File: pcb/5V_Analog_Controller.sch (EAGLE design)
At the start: 22 parts, among them J1 POWER, Q1 AO3400, Q2 AO3400, U1 ESP32-PICO-MINI-02, U2 AP2112K, X1 PROG, X2 SS-52100-001, X3 SS-52100-001, X5 BOOT, X6 RESET

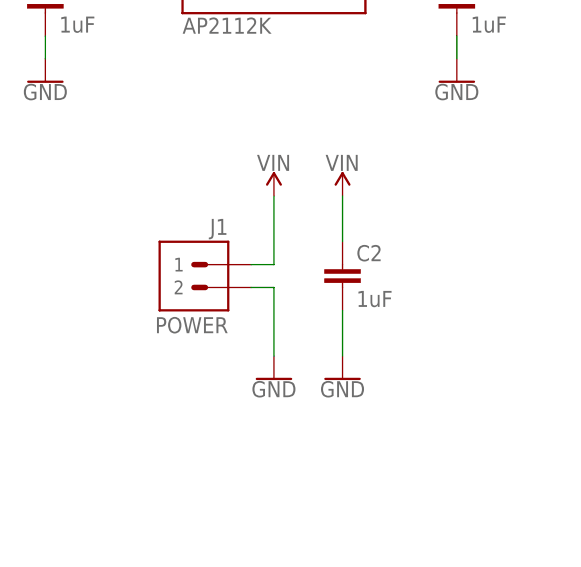
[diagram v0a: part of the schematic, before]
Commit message: Switch to input power jack
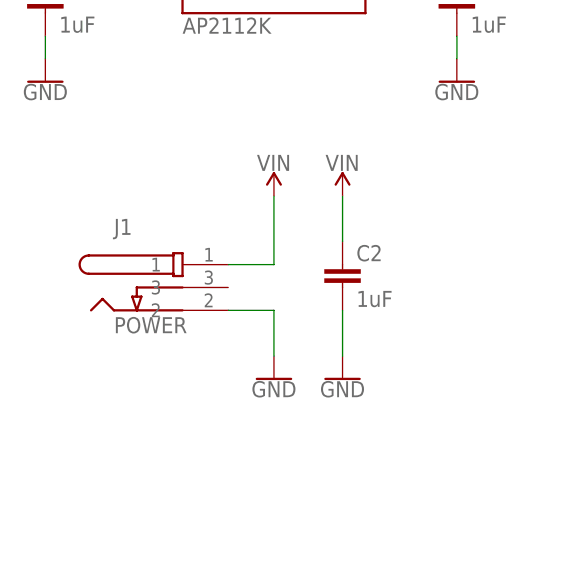
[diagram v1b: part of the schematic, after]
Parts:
- J1: device M2M-Connectors:TERMINAL-1X02-2.54P -> M2M-Connectors:XKB-DC-005-5A-2.0
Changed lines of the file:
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@@
 <part name="GND10" library="M2M-Power" deviceset="GND" device=""/>
 <part name="SUPPLY6" library="M2M-Power" deviceset="VCC" device=""/>
-<part name="J1" library="M2M-Connectors" deviceset="TERMINAL-1X02-2.54" device="P" value="POWER"/>
+<part name="J1" library="M2M-Connectors" deviceset="XKB-DC-005-5A-2.0" device="" value="POWER"/>
 <part name="U2" library="M2M-IC" deviceset="REGULATOR-AP2112K" device="K-SOT23-5" value="AP2112K"/>
 <part name="SUPPLY2" library="M2M-Power" deviceset="VIN" device=""/>
@@
 <attribute name="VALUE" x="160.02" y="160.274" size="1.778" layer="96" align="bottom-center"/>
 </instance>
-<instance part="J1" gate="G$1" x="43.18" y="111.76" smashed="yes" rot="MR0">
-<attribute name="VALUE" x="45.72" y="106.68" size="1.778" layer="96" rot="MR0"/>
-<attribute name="NAME" x="45.72" y="117.602" size="1.778" layer="95" rot="MR0"/>
+<instance part="J1" gate="G$1" x="35.56" y="111.76" smashed="yes">
+<attribute name="VALUE" x="33.02" y="106.68" size="1.778" layer="96"/>
+<attribute name="NAME" x="33.02" y="117.602" size="1.778" layer="95"/>
 </instance>
 <instance part="U2" gate="G$1" x="50.8" y="147.32" smashed="yes">
@@
 <segment>
 <pinref part="GND6" gate="1" pin="GND"/>
-<wire x1="48.26" y1="111.76" x2="50.8" y2="111.76" width="0.1524" layer="91"/>
-<wire x1="50.8" y1="111.76" x2="50.8" y2="104.14" width="0.1524" layer="91"/>
+<wire x1="45.72" y1="109.22" x2="50.8" y2="109.22" width="0.1524" layer="91"/>
+<wire x1="50.8" y1="109.22" x2="50.8" y2="104.14" width="0.1524" layer="91"/>
 <pinref part="J1" gate="G$1" pin="2"/>
 </segment>
@@
 <net name="VIN" class="0">
 <segment>
-<wire x1="48.26" y1="114.3" x2="50.8" y2="114.3" width="0.1524" layer="91"/>
+<wire x1="45.72" y1="114.3" x2="50.8" y2="114.3" width="0.1524" layer="91"/>
 <wire x1="50.8" y1="114.3" x2="50.8" y2="121.92" width="0.1524" layer="91"/>
 <pinref part="J1" gate="G$1" pin="1"/>

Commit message: Add reverse power protection for internal circuits
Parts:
- added D1: B5819LW, M2M-DiscreteSemi:DIODE-SCHOTTKYSOD-123
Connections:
- new net VSW: D1.A, F1.1, F2.1, J1.1
- net VIN: now also D1.C; no longer F1.1, F2.1, J1.1
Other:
- moved on the sheet: J1
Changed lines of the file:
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@@
 <part name="GND11" library="M2M-Power" deviceset="GND" device=""/>
 <part name="SUPPLY8" library="M2M-Power" deviceset="VCC" device=""/>
-<part name="SUPPLY3" library="M2M-Power" deviceset="VIN" device=""/>
-<part name="SUPPLY4" library="M2M-Power" deviceset="VIN" device=""/>
 <part name="SUPPLY5" library="M2M-Power" deviceset="VIN" device=""/>
 <part name="R3" library="M2M-Passives" deviceset="RESISTOR" device="0603" value="10K"/>
@@
 <part name="F1" library="M2M-Fuse" deviceset="PTC" device="JK-SMD300" value="JK-SMD300L-16"/>
 <part name="F2" library="M2M-Fuse" deviceset="PTC" device="JK-SMD300" value="JK-SMD300L-16"/>
+<part name="D1" library="M2M-DiscreteSemi" deviceset="DIODE-SCHOTTKY" device="SOD-123" value="B5819LW"/>
+<part name="SUPPLY3" library="M2M-Power" deviceset="VSW" device=""/>
+<part name="SUPPLY4" library="M2M-Power" deviceset="VSW" device=""/>
+<part name="SUPPLY11" library="M2M-Power" deviceset="VSW" device=""/>
 </parts>
 <sheets>
@@
 <attribute name="VALUE" x="160.02" y="160.274" size="1.778" layer="96" align="bottom-center"/>
 </instance>
-<instance part="J1" gate="G$1" x="35.56" y="111.76" smashed="yes">
-<attribute name="VALUE" x="33.02" y="106.68" size="1.778" layer="96"/>
-<attribute name="NAME" x="33.02" y="117.602" size="1.778" layer="95"/>
+<instance part="J1" gate="G$1" x="20.32" y="111.76" smashed="yes">
+<attribute name="VALUE" x="17.78" y="106.68" size="1.778" layer="96"/>
+<attribute name="NAME" x="17.78" y="117.602" size="1.778" layer="95"/>
 </instance>
 <instance part="U2" gate="G$1" x="50.8" y="147.32" smashed="yes">
@@
 <attribute name="VALUE" x="71.12" y="157.734" size="1.778" layer="96" align="bottom-center"/>
 </instance>
-<instance part="SUPPLY3" gate="G$1" x="182.88" y="147.32" smashed="yes">
-<attribute name="VALUE" x="182.88" y="150.114" size="1.778" layer="96" align="bottom-center"/>
-</instance>
-<instance part="SUPPLY4" gate="G$1" x="182.88" y="91.44" smashed="yes">
-<attribute name="VALUE" x="182.88" y="94.234" size="1.778" layer="96" align="bottom-center"/>
-</instance>
 <instance part="SUPPLY5" gate="G$1" x="58.42" y="121.92" smashed="yes">
 <attribute name="VALUE" x="58.42" y="124.714" size="1.778" layer="96" align="bottom-center"/>
@@
 <attribute name="NAME" x="187.96" y="88.646" size="1.778" layer="95"/>
 <attribute name="VALUE" x="187.96" y="82.296" size="1.778" layer="95"/>
+</instance>
+<instance part="D1" gate="G$1" x="40.64" y="114.3" smashed="yes">
+<attribute name="NAME" x="36.83" y="116.078" size="1.778" layer="95"/>
+<attribute name="VALUE" x="36.83" y="110.744" size="1.778" layer="96"/>
+</instance>
+<instance part="SUPPLY3" gate="G$1" x="33.02" y="121.92" smashed="yes">
+<attribute name="VALUE" x="33.02" y="124.714" size="1.778" layer="96" align="bottom-center"/>
+</instance>
+<instance part="SUPPLY4" gate="G$1" x="182.88" y="147.32" smashed="yes">
+<attribute name="VALUE" x="182.88" y="150.114" size="1.778" layer="96" align="bottom-center"/>
+</instance>
+<instance part="SUPPLY11" gate="G$1" x="182.88" y="91.44" smashed="yes">
+<attribute name="VALUE" x="182.88" y="94.234" size="1.778" layer="96" align="bottom-center"/>
 </instance>
 </instances>
@@
 <segment>
 <pinref part="GND6" gate="1" pin="GND"/>
-<wire x1="45.72" y1="109.22" x2="50.8" y2="109.22" width="0.1524" layer="91"/>
+<wire x1="30.48" y1="109.22" x2="50.8" y2="109.22" width="0.1524" layer="91"/>
 <wire x1="50.8" y1="109.22" x2="50.8" y2="104.14" width="0.1524" layer="91"/>
 <pinref part="J1" gate="G$1" pin="2"/>
@@
 <net name="VIN" class="0">
 <segment>
-<wire x1="45.72" y1="114.3" x2="50.8" y2="114.3" width="0.1524" layer="91"/>
 <wire x1="50.8" y1="114.3" x2="50.8" y2="121.92" width="0.1524" layer="91"/>
-<pinref part="J1" gate="G$1" pin="1"/>
 <pinref part="SUPPLY2" gate="G$1" pin="VIN"/>
+<pinref part="D1" gate="G$1" pin="C"/>
+<wire x1="43.18" y1="114.3" x2="50.8" y2="114.3" width="0.1524" layer="91"/>
 </segment>
 <segment>
@@
 <pinref part="SUPPLY5" gate="G$1" pin="VIN"/>
 </segment>
-<segment>
-<pinref part="SUPPLY3" gate="G$1" pin="VIN"/>
+</net>
+<net name="N$5" class="0">
+<segment>
+<pinref part="X2" gate="G$1" pin="UVCC"/>
+<wire x1="208.28" y1="142.24" x2="195.58" y2="142.24" width="0.1524" layer="91"/>
+<pinref part="F1" gate="G$1" pin="2"/>
+</segment>
+</net>
+<net name="N$6" class="0">
+<segment>
+<pinref part="X3" gate="G$1" pin="UVCC"/>
+<wire x1="208.28" y1="86.36" x2="195.58" y2="86.36" width="0.1524" layer="91"/>
+<pinref part="F2" gate="G$1" pin="2"/>
+</segment>
+</net>
+<net name="VSW" class="0">
+<segment>
 <pinref part="F1" gate="G$1" pin="1"/>
 <wire x1="182.88" y1="147.32" x2="182.88" y2="142.24" width="0.1524" layer="91"/>
 <wire x1="182.88" y1="142.24" x2="185.42" y2="142.24" width="0.1524" layer="91"/>
-</segment>
-<segment>
-<pinref part="SUPPLY4" gate="G$1" pin="VIN"/>
+<pinref part="SUPPLY4" gate="G$1" pin="VSW"/>
+</segment>
+<segment>
 <pinref part="F2" gate="G$1" pin="1"/>
 <wire x1="182.88" y1="91.44" x2="182.88" y2="86.36" width="0.1524" layer="91"/>
 <wire x1="182.88" y1="86.36" x2="185.42" y2="86.36" width="0.1524" layer="91"/>
-</segment>
-</net>
-<net name="N$5" class="0">
-<segment>
-<pinref part="X2" gate="G$1" pin="UVCC"/>
-<wire x1="208.28" y1="142.24" x2="195.58" y2="142.24" width="0.1524" layer="91"/>
-<pinref part="F1" gate="G$1" pin="2"/>
-</segment>
-</net>
-<net name="N$6" class="0">
-<segment>
-<pinref part="X3" gate="G$1" pin="UVCC"/>
-<wire x1="208.28" y1="86.36" x2="195.58" y2="86.36" width="0.1524" layer="91"/>
-<pinref part="F2" gate="G$1" pin="2"/>
-</segment>
-</net>
+<pinref part="SUPPLY11" gate="G$1" pin="VSW"/>
+</segment>
+<segment>
+<pinref part="SUPPLY3" gate="G$1" pin="VSW"/>
+<pinref part="J1" gate="G$1" pin="1"/>
+<wire x1="33.02" y1="121.92" x2="33.02" y2="114.3" width="0.1524" layer="91"/>
+<wire x1="33.02" y1="114.3" x2="30.48" y2="114.3" width="0.1524" layer="91"/>
+<pinref part="D1" gate="G$1" pin="A"/>
+<wire x1="33.02" y1="114.3" x2="38.1" y2="114.3" width="0.1524" layer="91"/>
+<junction x="33.02" y="114.3"/>
+</segment>
+</net>

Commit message: Add second PTC footprint
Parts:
- added F3, F4: JK-SMD300L-16, M2M-Fuse:PTCJK-SMD300
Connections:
- net N$5: now also F3.2
- net N$6: now also F4.2
- net VSW: now also F3.1, F4.1
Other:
- moved on the sheet: F1, F2
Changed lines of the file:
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@@
 <part name="SUPPLY4" library="M2M-Power" deviceset="VSW" device=""/>
 <part name="SUPPLY11" library="M2M-Power" deviceset="VSW" device=""/>
+<part name="F3" library="M2M-Fuse" deviceset="PTC" device="JK-SMD300" value="JK-SMD300L-16"/>
+<part name="F4" library="M2M-Fuse" deviceset="PTC" device="JK-SMD300" value="JK-SMD300L-16"/>
 </parts>
 <sheets>
@@
 <attribute name="VALUE" x="66.04" y="76.454" size="1.778" layer="96" align="bottom-center"/>
 </instance>
-<instance part="F1" gate="G$1" x="190.5" y="142.24" smashed="yes">
-<attribute name="NAME" x="187.96" y="144.526" size="1.778" layer="95"/>
-<attribute name="VALUE" x="187.96" y="138.176" size="1.778" layer="95"/>
-</instance>
-<instance part="F2" gate="G$1" x="190.5" y="86.36" smashed="yes">
-<attribute name="NAME" x="187.96" y="88.646" size="1.778" layer="95"/>
-<attribute name="VALUE" x="187.96" y="82.296" size="1.778" layer="95"/>
+<instance part="F1" gate="G$1" x="187.96" y="142.24" smashed="yes">
+<attribute name="NAME" x="185.42" y="144.526" size="1.778" layer="95"/>
+<attribute name="VALUE" x="185.42" y="138.176" size="1.778" layer="95"/>
+</instance>
+<instance part="F2" gate="G$1" x="187.96" y="86.36" smashed="yes">
+<attribute name="NAME" x="185.42" y="88.646" size="1.778" layer="95"/>
+<attribute name="VALUE" x="185.42" y="82.296" size="1.778" layer="95"/>
 </instance>
 <instance part="D1" gate="G$1" x="40.64" y="114.3" smashed="yes">
@@
 <attribute name="VALUE" x="33.02" y="124.714" size="1.778" layer="96" align="bottom-center"/>
 </instance>
-<instance part="SUPPLY4" gate="G$1" x="182.88" y="147.32" smashed="yes">
-<attribute name="VALUE" x="182.88" y="150.114" size="1.778" layer="96" align="bottom-center"/>
-</instance>
-<instance part="SUPPLY11" gate="G$1" x="182.88" y="91.44" smashed="yes">
-<attribute name="VALUE" x="182.88" y="94.234" size="1.778" layer="96" align="bottom-center"/>
+<instance part="SUPPLY4" gate="G$1" x="180.34" y="152.4" smashed="yes">
+<attribute name="VALUE" x="180.34" y="155.194" size="1.778" layer="96" align="bottom-center"/>
+</instance>
+<instance part="SUPPLY11" gate="G$1" x="180.34" y="96.52" smashed="yes">
+<attribute name="VALUE" x="180.34" y="99.314" size="1.778" layer="96" align="bottom-center"/>
+</instance>
+<instance part="F3" gate="G$1" x="187.96" y="149.86" smashed="yes">
+<attribute name="NAME" x="185.42" y="152.146" size="1.778" layer="95"/>
+<attribute name="VALUE" x="185.42" y="145.796" size="1.778" layer="95"/>
+</instance>
+<instance part="F4" gate="G$1" x="187.96" y="93.98" smashed="yes">
+<attribute name="NAME" x="185.42" y="96.266" size="1.778" layer="95"/>
+<attribute name="VALUE" x="185.42" y="89.916" size="1.778" layer="95"/>
 </instance>
 </instances>
@@
 <segment>
 <pinref part="X2" gate="G$1" pin="UVCC"/>
-<wire x1="208.28" y1="142.24" x2="195.58" y2="142.24" width="0.1524" layer="91"/>
+<wire x1="208.28" y1="142.24" x2="205.74" y2="142.24" width="0.1524" layer="91"/>
 <pinref part="F1" gate="G$1" pin="2"/>
+<pinref part="F3" gate="G$1" pin="2"/>
+<wire x1="205.74" y1="142.24" x2="193.04" y2="142.24" width="0.1524" layer="91"/>
+<wire x1="193.04" y1="149.86" x2="205.74" y2="149.86" width="0.1524" layer="91"/>
+<wire x1="205.74" y1="149.86" x2="205.74" y2="142.24" width="0.1524" layer="91"/>
+<junction x="205.74" y="142.24"/>
 </segment>
 </net>
@@
 <segment>
 <pinref part="X3" gate="G$1" pin="UVCC"/>
-<wire x1="208.28" y1="86.36" x2="195.58" y2="86.36" width="0.1524" layer="91"/>
+<wire x1="208.28" y1="86.36" x2="205.74" y2="86.36" width="0.1524" layer="91"/>
 <pinref part="F2" gate="G$1" pin="2"/>
+<pinref part="F4" gate="G$1" pin="2"/>
+<wire x1="205.74" y1="86.36" x2="193.04" y2="86.36" width="0.1524" layer="91"/>
+<wire x1="193.04" y1="93.98" x2="205.74" y2="93.98" width="0.1524" layer="91"/>
+<wire x1="205.74" y1="93.98" x2="205.74" y2="86.36" width="0.1524" layer="91"/>
+<junction x="205.74" y="86.36"/>
 </segment>
 </net>
@@
 <segment>
 <pinref part="F1" gate="G$1" pin="1"/>
-<wire x1="182.88" y1="147.32" x2="182.88" y2="142.24" width="0.1524" layer="91"/>
-<wire x1="182.88" y1="142.24" x2="185.42" y2="142.24" width="0.1524" layer="91"/>
+<wire x1="180.34" y1="152.4" x2="180.34" y2="149.86" width="0.1524" layer="91"/>
+<wire x1="180.34" y1="149.86" x2="180.34" y2="142.24" width="0.1524" layer="91"/>
+<wire x1="180.34" y1="142.24" x2="182.88" y2="142.24" width="0.1524" layer="91"/>
 <pinref part="SUPPLY4" gate="G$1" pin="VSW"/>
+<pinref part="F3" gate="G$1" pin="1"/>
+<wire x1="180.34" y1="149.86" x2="182.88" y2="149.86" width="0.1524" layer="91"/>
+<junction x="180.34" y="149.86"/>
 </segment>
 <segment>
 <pinref part="F2" gate="G$1" pin="1"/>
-<wire x1="182.88" y1="91.44" x2="182.88" y2="86.36" width="0.1524" layer="91"/>
-<wire x1="182.88" y1="86.36" x2="185.42" y2="86.36" width="0.1524" layer="91"/>
+<wire x1="180.34" y1="96.52" x2="180.34" y2="93.98" width="0.1524" layer="91"/>
+<wire x1="180.34" y1="93.98" x2="180.34" y2="86.36" width="0.1524" layer="91"/>
+<wire x1="180.34" y1="86.36" x2="182.88" y2="86.36" width="0.1524" layer="91"/>
 <pinref part="SUPPLY11" gate="G$1" pin="VSW"/>
-</segment>
-<segment>
+<pinref part="F4" gate="G$1" pin="1"/>
+<wire x1="180.34" y1="93.98" x2="182.88" y2="93.98" width="0.1524" layer="91"/>
+<junction x="180.34" y="93.98"/>
+</segment>
+<segment>
